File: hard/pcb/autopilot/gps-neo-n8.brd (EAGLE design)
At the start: 99.9 x 65 mm, 18 parts, among them Q1 IRLML5203, T3 BC848

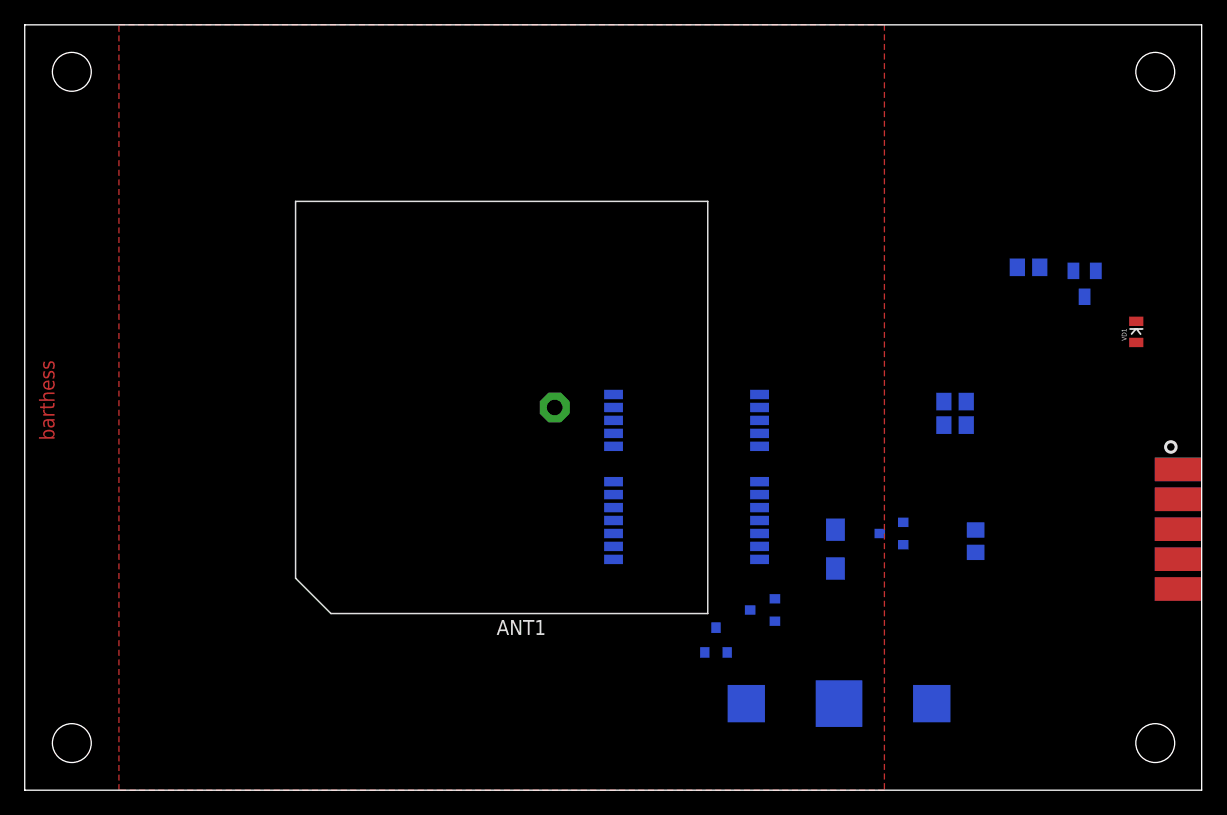
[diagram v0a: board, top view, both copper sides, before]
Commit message: update gps NEO board
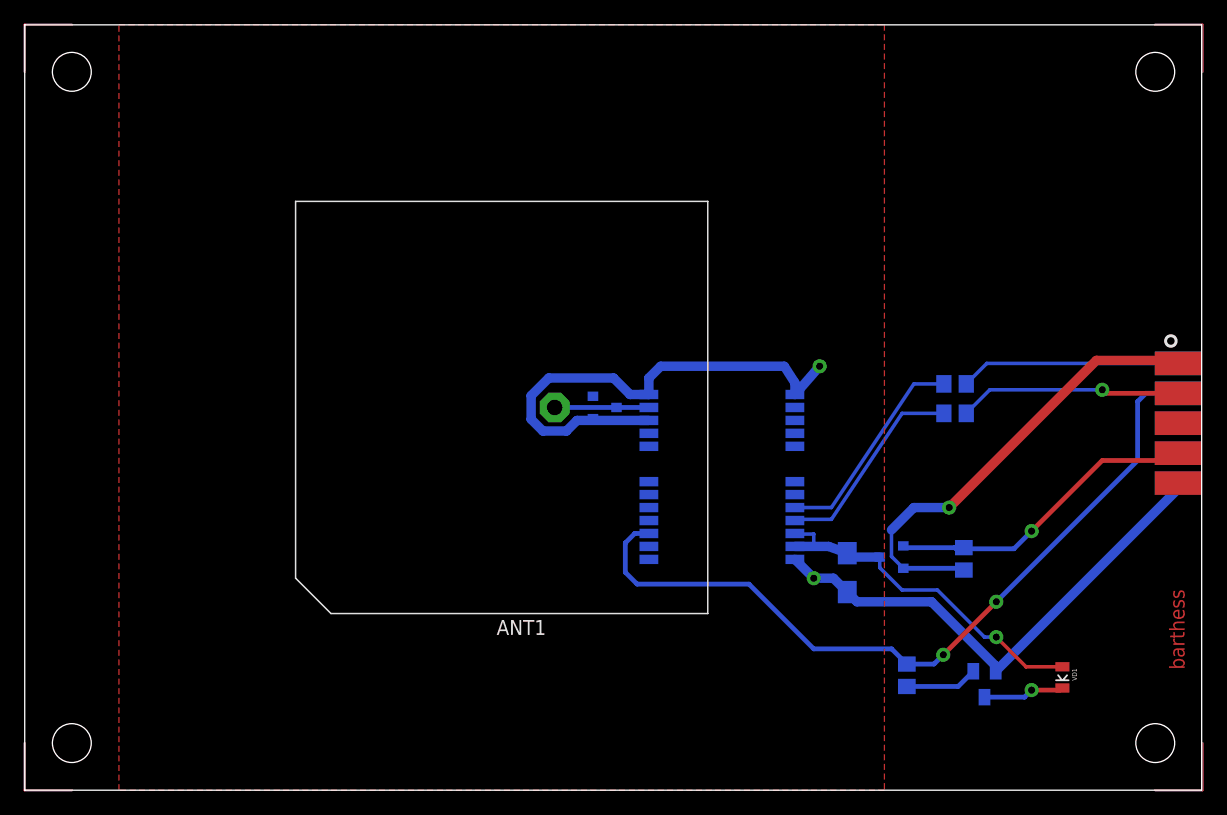
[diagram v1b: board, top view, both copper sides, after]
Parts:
- removed BAT1: (no value), SparkFun:BATTCON_12MM
- removed VD2, VD3: BAR43, barthess:SOT23-3
- added Q2: IRLML5203, transistor-power:MICRO3
- added U$2: (no value), barthess:LOGO_CHIBIOS_SIGNAL
- moved R1 36.2 mm to (74.9, 9.76), turned to 90 degrees
- moved T3 35.0 mm to (81.5, 9.00)
- moved VD1 30.0 mm to (88.1, 9.58), turned to 270 degrees
- moved XP1 9.00 mm to (98.0, 31.2)
- moved U$1 3.00 mm to (65.3, 34.6)
- moved C1 2.24 mm to (69.8, 18.5)
- moved Q1 2.00 mm to (73.6, 19.8)
- moved R26 1.80 mm to (79.7, 19.6)
- moved R3 1.50 mm to (79.0, 34.5)
- moved R2 1.00 mm to (79.0, 32.0)
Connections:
- removed net N$5: BAT1.PWR@1, VD2.1
- removed net N$6: U$1.22, VD2.3, VD3.3
- net GND: no longer BAT1.GND
- net GPS_3.3V: now also U$1.22; no longer VD3.1
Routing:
- net GND: track 0.00 -> 86.8 mm, vias 0 -> 2
- net PPS: track 0.00 -> 67.5 mm, vias 0 -> 2
- net 3.3V: track 0.00 -> 39.3 mm, vias 0 -> 1
- net GPS_3.3V: track 0.00 -> 31.6 mm, vias 0 -> 1
- net GPS_ENABLE: track 0.00 -> 27.6 mm, vias 0 -> 1
- net TO_GPS: track 0.00 -> 19.0 mm, vias 0 -> 1
- net FROM_GPS: track 0.00 -> 18.7 mm
- net N$8: track 0.00 -> 18.3 mm
- net N$4: track 0.00 -> 17.5 mm
- net N$9: track 0.00 -> 8.00 mm
- net N$7: track 0.00 -> 8.00 mm
- net N$6: track 0.00 -> 8.00 mm
- net N$5: track 0.00 -> 8.00 mm
- net N$2: track 0.00 -> 8.00 mm
- net N$13: track 0.00 -> 8.00 mm
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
